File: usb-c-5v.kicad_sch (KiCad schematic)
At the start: 11 parts, among them J2 KH-TYPE-C-16P (Kinghelm), U2 AP2112K-3.3

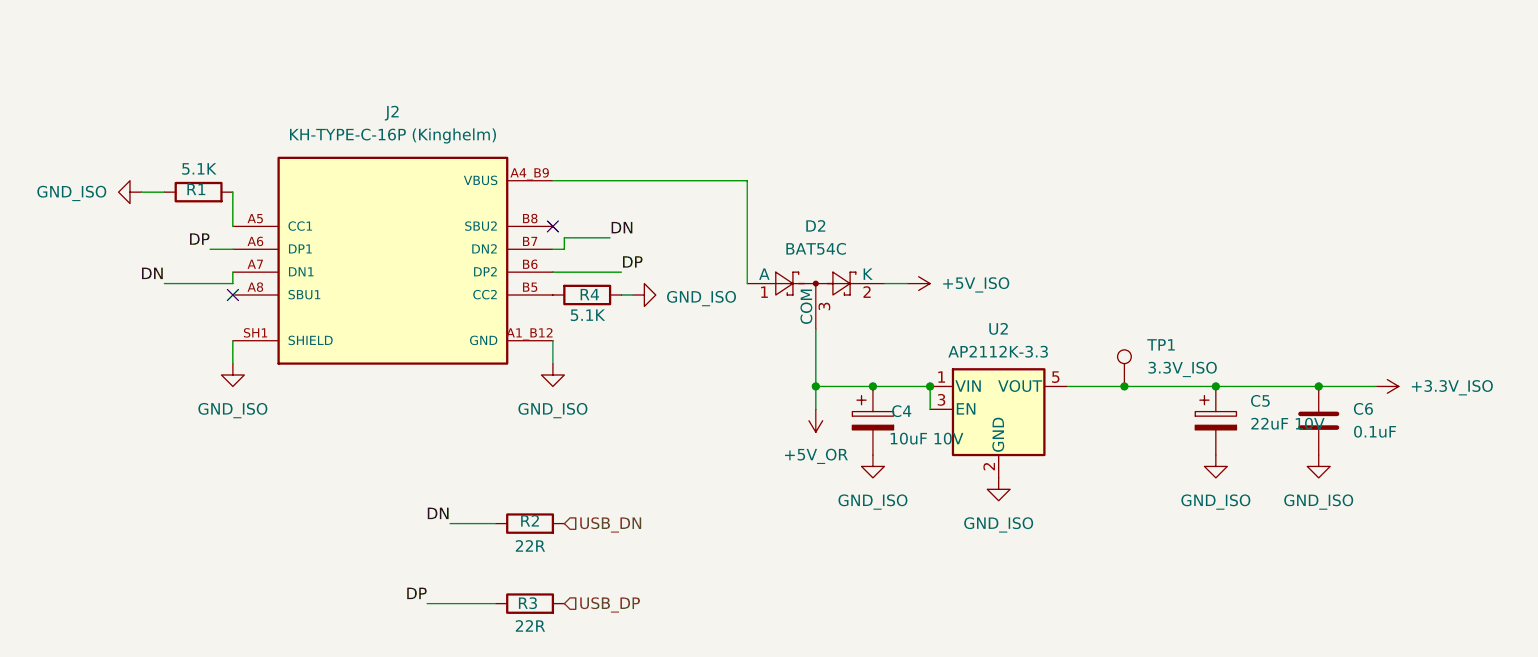
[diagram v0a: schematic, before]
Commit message: Updated USB to switch from USB-C to Micro
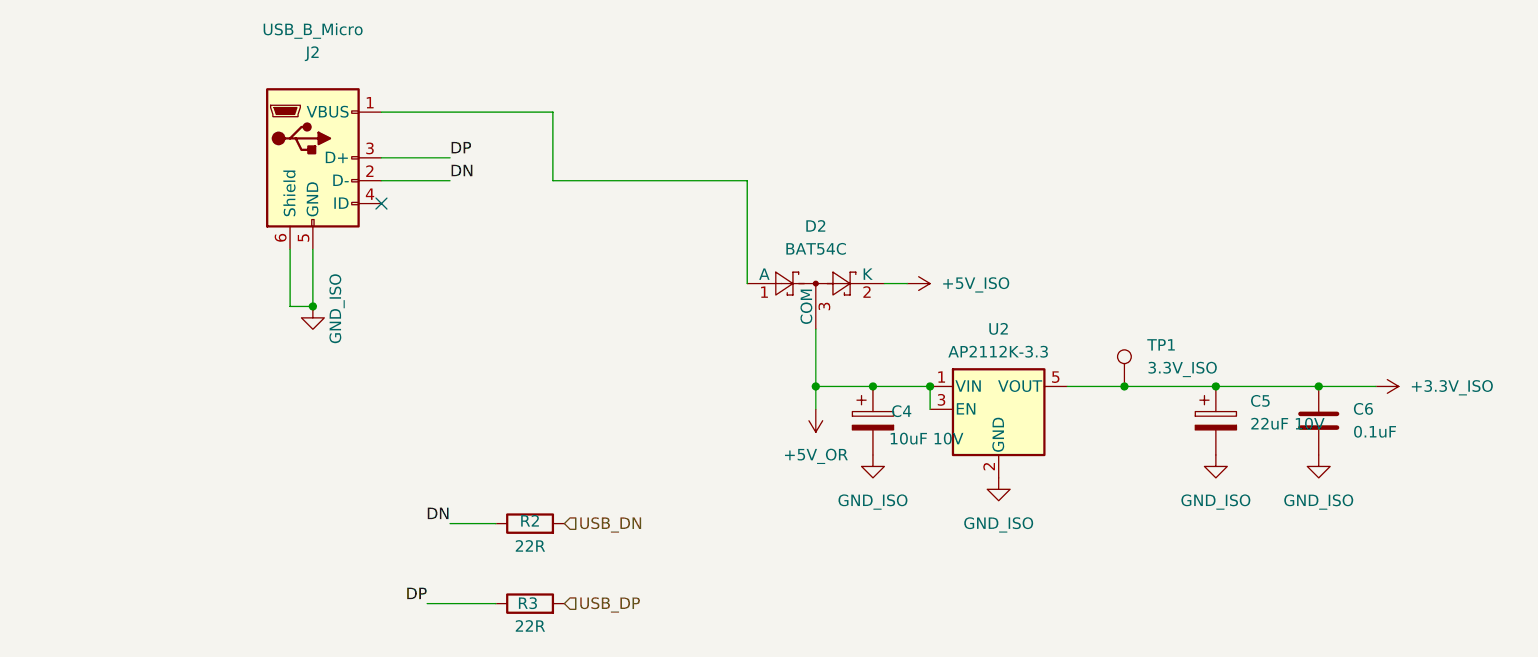
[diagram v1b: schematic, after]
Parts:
- removed J2: KH-TYPE-C-16P (Kinghelm), barn_shade_controller:KINGHELM_KH-TYPE-C-16P, symbol KH-TYPE-C-16P:KH-TYPE-C-16P
- removed R1, R4: 5.1K, Resistor_SMD:R_0402_1005Metric, symbol Device:R
- added J2: USB_B_Micro, Connector_USB:USB_Micro-B_XKB_U254-051T-4BH83-F1S, symbol Connector:USB_B_Micro
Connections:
- net DN: now also J2.2 (D-)
- net DP: now also J2.3 (D+)
- net GND renamed GND_ISO
- net GND_ISO: now also J2.5 (GND), J2.6 (Shield)
- net VBUS: no longer names the net of D2.1 (A)
- net VBUS: now also J2.1 (VBUS)
- no-connect marks 2 -> 1

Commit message: Updating routing with new terminal block
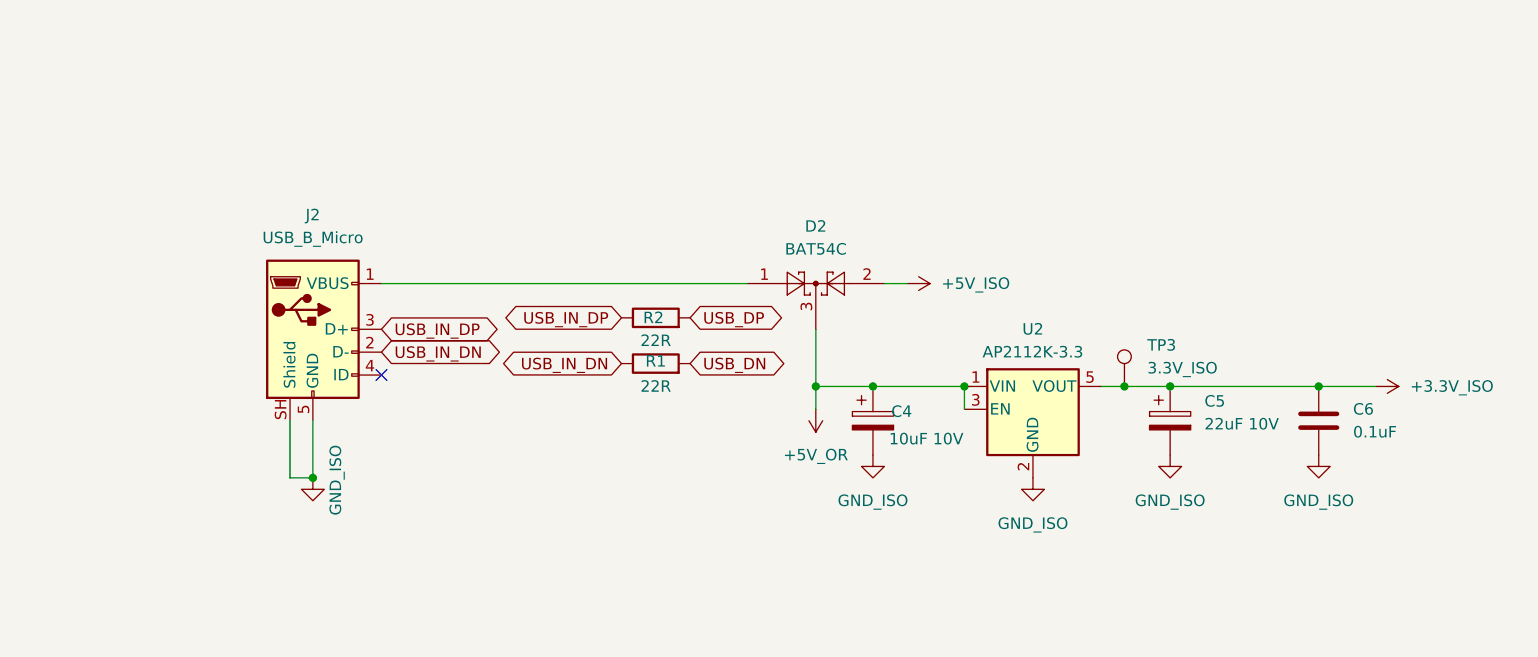
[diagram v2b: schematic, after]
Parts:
- removed D2: BAT54C, Package_TO_SOT_SMD:SOT-23, symbol Diode:BAT54S
- added D2: BAT54C, Package_TO_SOT_SMD:SOT-23, symbol Diode:BAT54C
- J2: LCSC C397452 -> (none)
- TP3: renamed from TP1; footprint barn_shade_controller:TestPoint_Pad_D1.0mm_No_SolderMask -> TestPoint:TestPoint_Pad_D1.0mm
- renumbered R2 to R1, R3 to R2
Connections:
- net +5V_ISO: now also D2.2
- net +5V_OR: now also D2.3
- net GND_ISO: now also J2.SH (Shield); no longer J2.6 (Shield)
- net at J2.1 (VBUS): now also D2.1
- net DN renamed USB_IN_DN
- net DP renamed USB_IN_DP
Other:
- moved on the sheet: C5, R1, R2, U2
